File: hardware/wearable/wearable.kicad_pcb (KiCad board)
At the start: 4 copper layers, 30 x 70 mm, 73 parts, among them IC1 LM4041CILPR, IC2 INA828IDR, IC3 MAX30102EFD+T, IC4 TPS63001DRCT, IC5 OPA2350UA, IC6 TPS62293DRVR, J1 Conn_02x05_Odd_Even, J2 Conn_01x04_Pin, SW1 SW_Push, SW2 SW_SPDT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

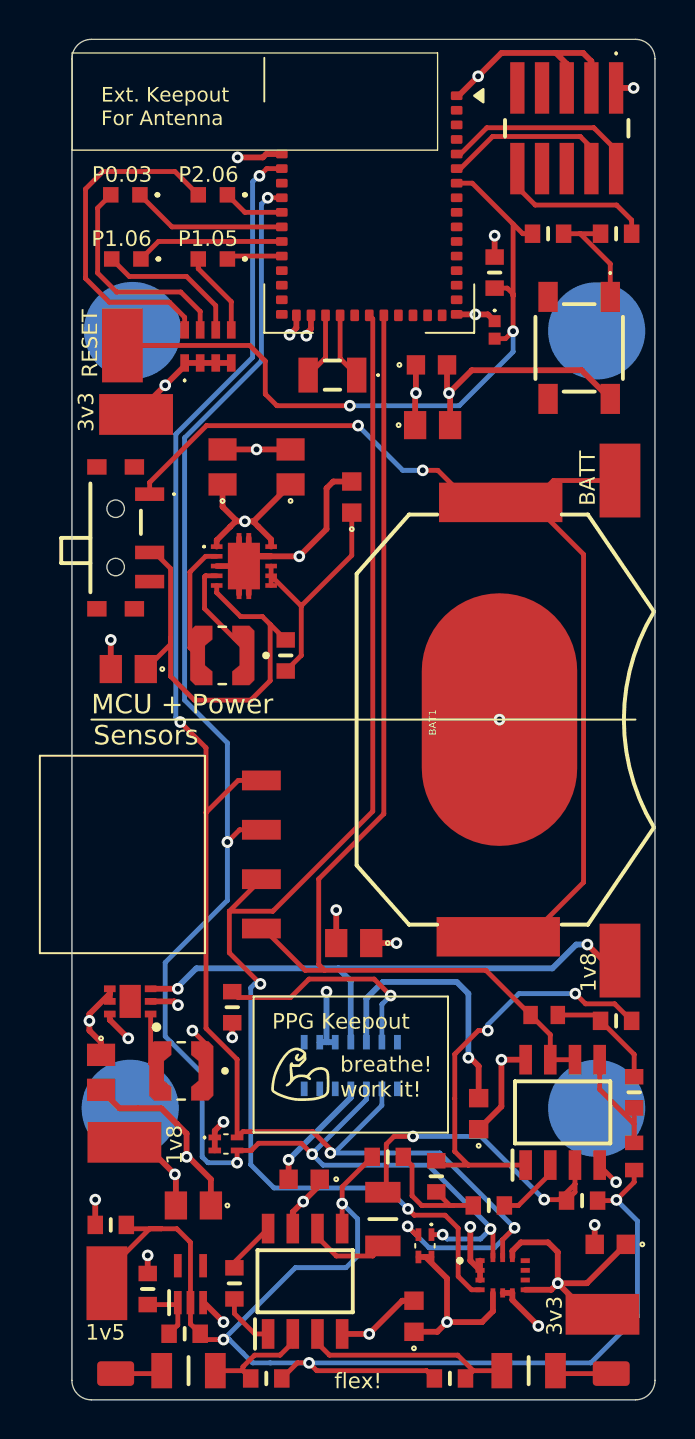
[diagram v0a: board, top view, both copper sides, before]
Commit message: ahhhhhhhhhhhhhhhhhhhhhhh firmware is no longer a submodule per peer request... thanks brianna...
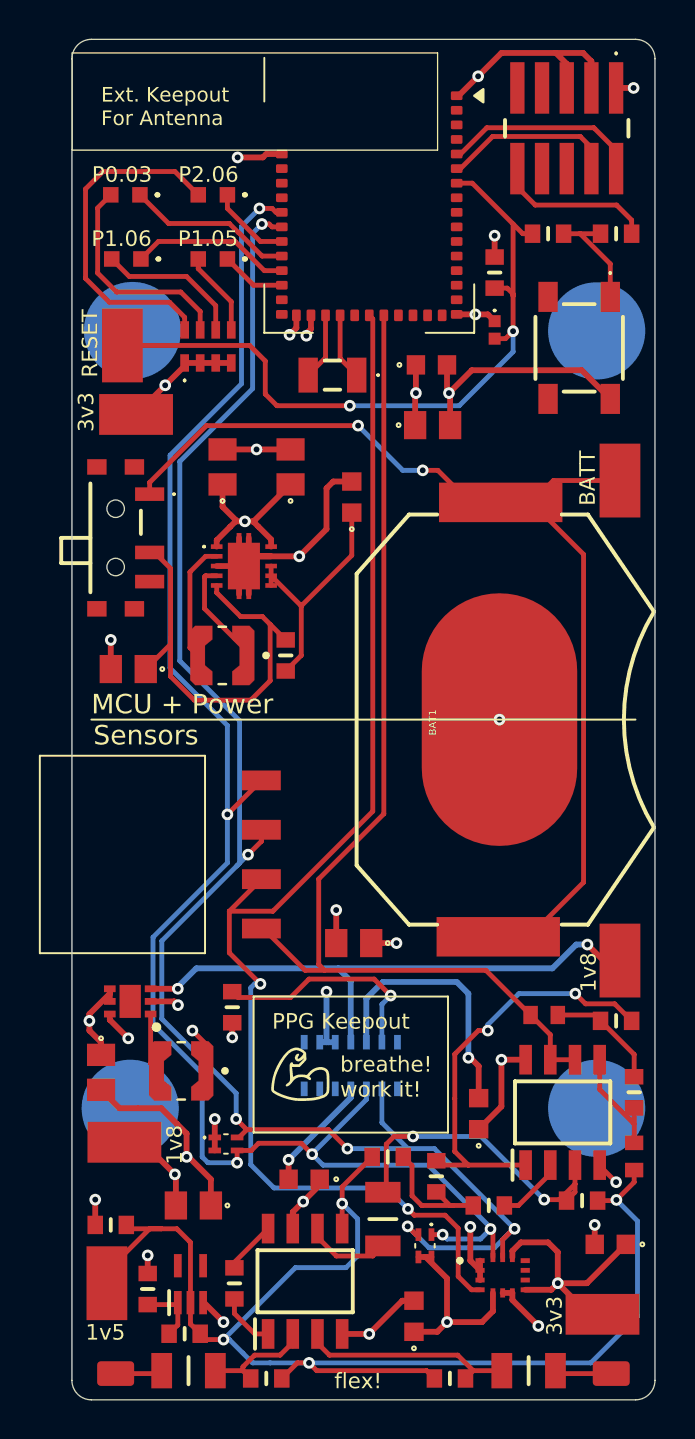
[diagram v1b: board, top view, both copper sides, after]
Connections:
- D1 pad 1: P1.11 -> P1.13
- D2 pad 1: P1.12 -> P1.14
- D3 pad 1: P1.13 -> P0.04
- D4 pad 1: P1.14 -> P1.08
- IC3 pad 2: P2.06 -> P1.12
- IC3 pad 3: P0.03 -> P1.11
- J2 pad 3: P0.03 -> P1.12
- J2 pad 4: P2.06 -> P1.11
- RN2 pad 3: P0.03 -> P1.11
- RN2 pad 4: P2.06 -> P1.12
- RN3 pad 1: P0.03 -> P1.11
- RN3 pad 2: P2.06 -> P1.12
- U5 pad 13: P2.06 -> P1.12
- U5 pad 14: P0.03 -> P1.11
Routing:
- net P2.06: track 87.5 -> 0.00 mm, vias 5 -> 0
- net P0.03: track 84.2 -> 0.00 mm, vias 6 -> 0
- net P1.11: track 3.17 -> 85.5 mm, vias 0 -> 6
- net P1.12: track 7.98 -> 85.7 mm, vias 0 -> 6
- net P0.04: track 0.00 -> 8.24 mm
- net P1.14: track 2.86 -> 8.60 mm
- net P1.08: track 0.00 -> 3.57 mm
- net P1.13: track 7.62 -> 4.20 mm
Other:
- board text added: "Brianna Aguilar Tyler Tekin Joanna Enyioke Mario Ramirez"
